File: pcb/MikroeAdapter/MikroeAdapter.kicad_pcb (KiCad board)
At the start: 2 copper layers, 32.8 x 86.9 mm, 32 parts, among them CON1 MIKROBUS_HOST_CONN, J1 Conn_01x03, J2 Screw_Terminal_01x02, J3 Conn_01x02, J4 Screw_Terminal_01x12, J5 Screw_Terminal_01x02, U1 MP2331HGTL-Z, U2 ATtiny1604-SS, U3 THVD1450D

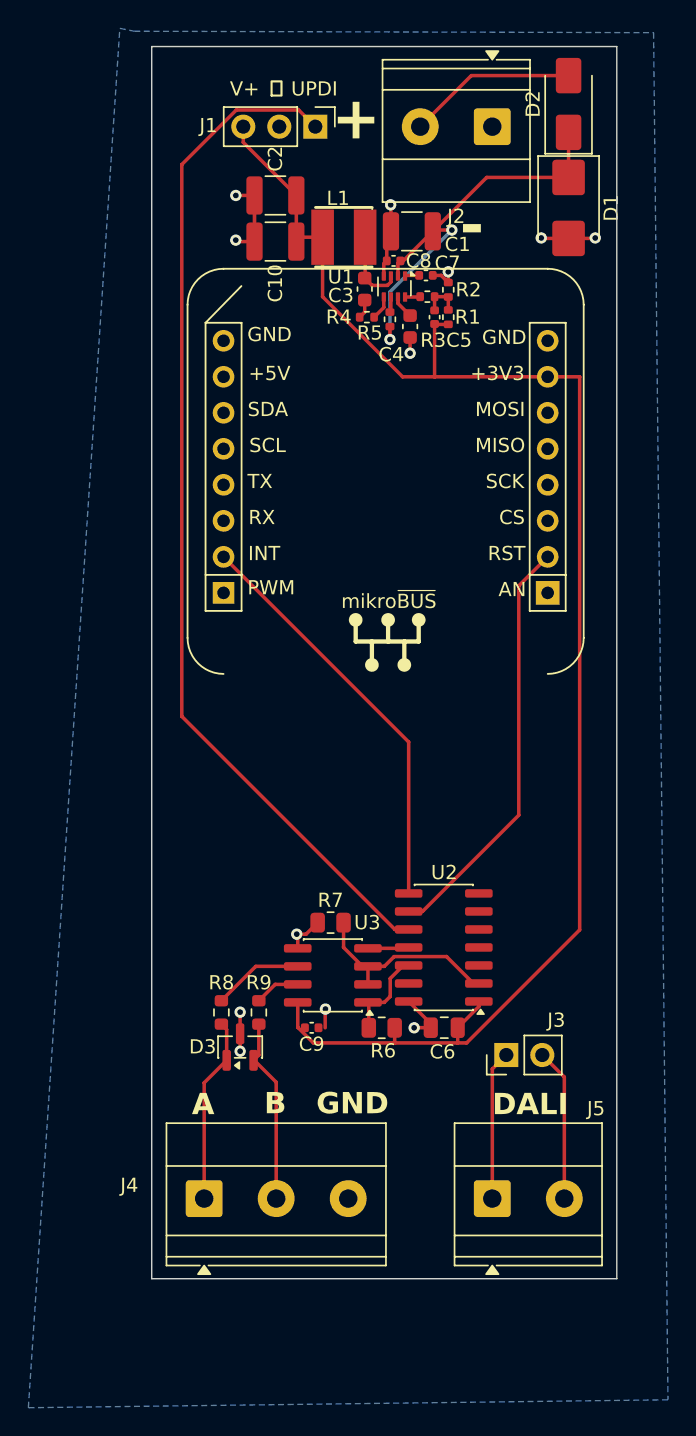
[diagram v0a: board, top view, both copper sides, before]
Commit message: mbq: embed the status pair in the slot; make MBQ_CMD_REGS load-bearing
The previous commit introduced two declarations that nothing used, in a
change whose purpose was removing dead code:

  - mbq_slot_status_t declared the [status | response8] wire pair, while
    mbq_slot_t separately repeated both fields. Two definitions of one
    layout, free to drift.
  - MBQ_CMD_REGS documented that a submit's length is in REGISTERS — the
    units confusion behind the two-slot bug — while modbus.c went on
    deriving first_slot and n_slots from a literal 2.

Fix both by use rather than deletion. mbq_slot_t now embeds
mbq_slot_status_t as `st`, so the in-memory and wire layouts cannot
disagree, and submit_window() derives its slot arithmetic (and its
boundary/length validation) from MBQ_CMD_REGS.

Ordering is unchanged: mbq_complete still writes st.response8 before
st.status under the same fence the status read uses. sizeof(mbq_slot_t)
== 8 still asserts. Flash is identical at 10078 B.

Verified on hardware: 400-pair soak, 14.76 pairs/s, VERDICT clean —
400 query-correct, 0 stale, 0 wrong, 0 lost, 0 out-of-order.

Co-Authored-By: Claude Opus 5 (1M context) <noreply@anthropic.com>
Claude-Session: https://claude.ai/code/session_01STSZT2DguJ8ntaDTJXvk1d
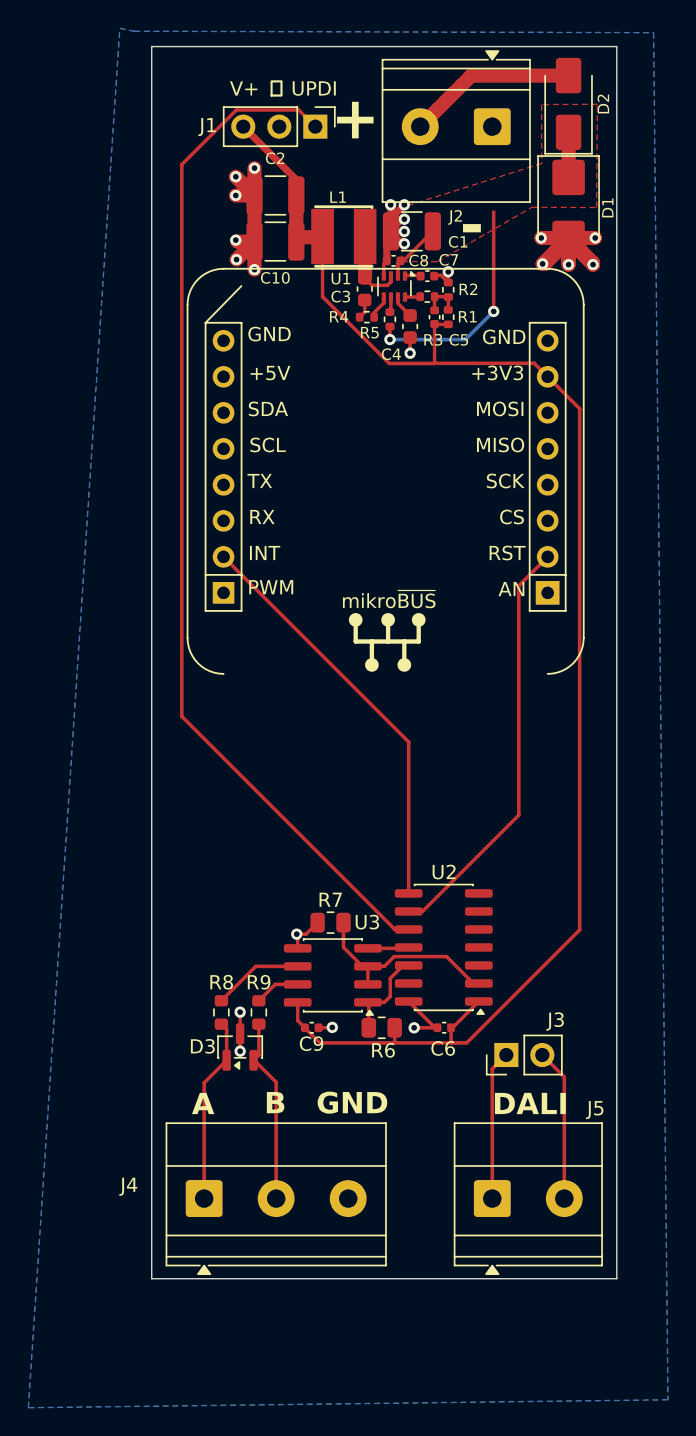
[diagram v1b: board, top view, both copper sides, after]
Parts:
- C6: footprint Capacitor_SMD:C_0805_2012Metric -> Capacitor_SMD:C_0402_1005Metric
- moved C7 0.11 mm to (69.4, 66.2)
- moved L1 0.05 mm to (63.6, 63.4)
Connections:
- net Net-(U1-PG) renamed /PG
- net Net-(U1-SW) renamed /SW
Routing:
- net GND: track 28.8 -> 59.1 mm, vias 12 -> 23
- net /V_IN: track 30.7 -> 23.9 mm
- net VCC: track 110.1 -> 107.6 mm
- added copper zone on F.Cu, net /V_IN
